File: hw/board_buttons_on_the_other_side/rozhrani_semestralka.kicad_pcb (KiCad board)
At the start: 2 copper layers, 152 x 38.6 mm, 64 parts, among them P1 DISPLAY_CONN, P2 DISPLAY_VCC_CON, P3 USB_B, U1 MCP2210, U2 MIC5504-3.3, U3 Joystick, U4 LM239, U5 CD4532, U6 NPIC6C596, U7 NE555, U8 PB6149L, U9 PB6149L

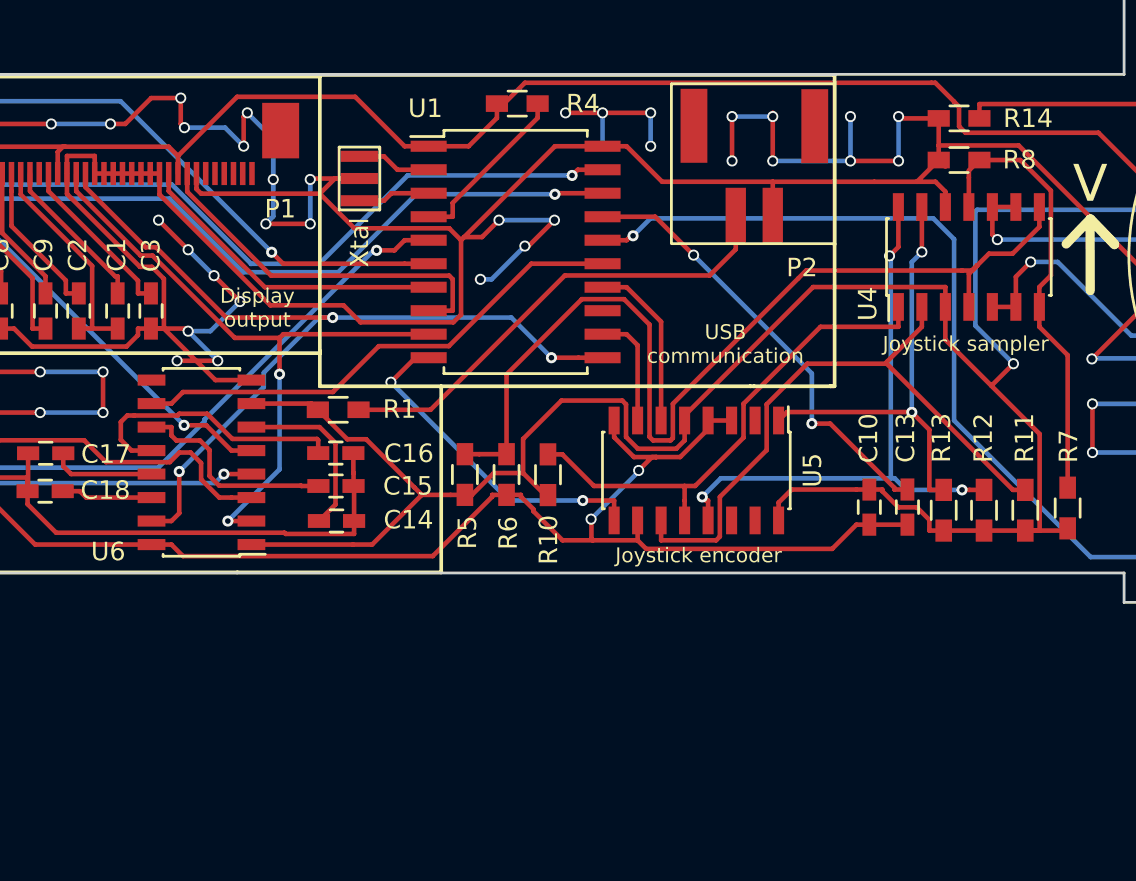
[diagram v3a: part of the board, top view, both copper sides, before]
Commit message: unconnected central button
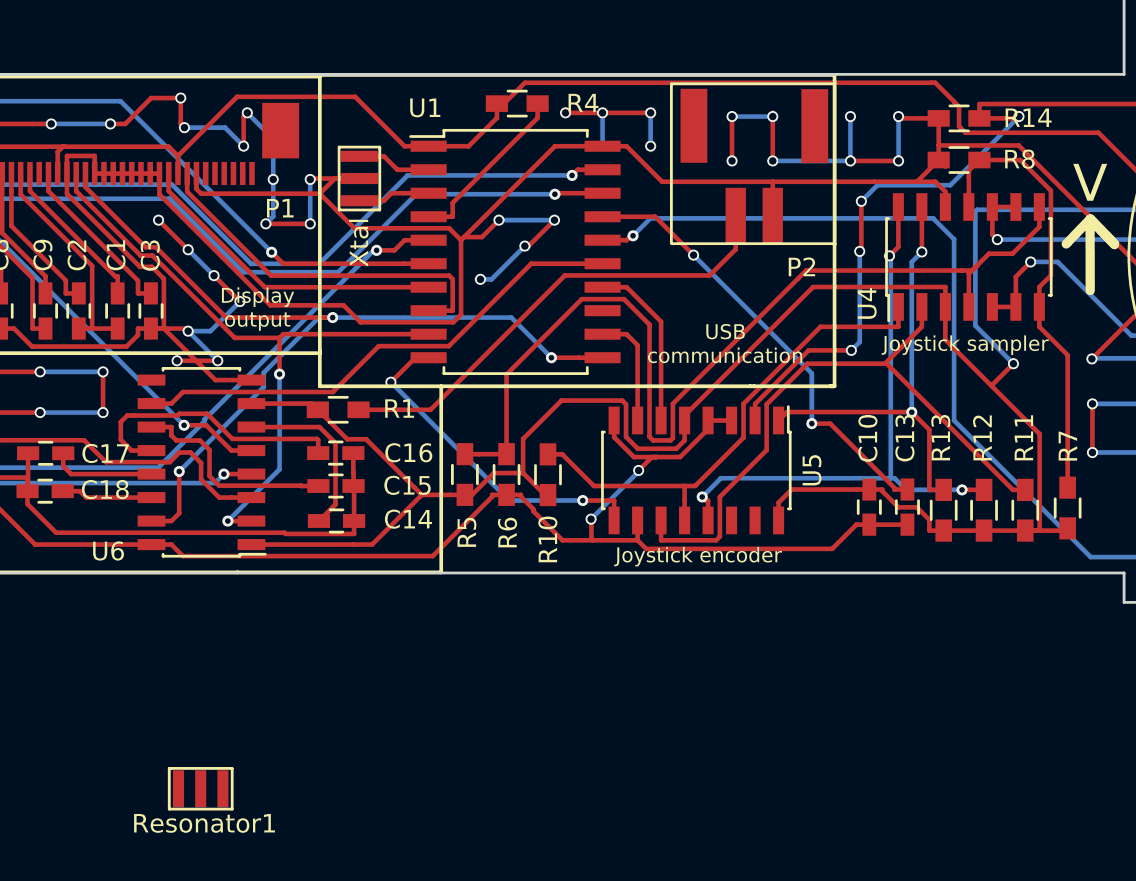
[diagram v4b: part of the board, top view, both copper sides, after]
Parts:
- added Resonator1: 12MHz, pcb:resonator12MHz, F.Cu at (150.7, 131.3)
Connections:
- R14 pad 2: Net-(R14-Pad2) -> /JOY_C
- U3 pad 1: Net-(R14-Pad2) -> /JOY_C
- U3 pad 2: Net-(R14-Pad2) -> /JOY_C
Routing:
- net /JOY_C: track 0.00 -> 54.6 mm, vias 0 -> 4
- net Net-(R14-Pad2): track 26.4 -> 0.00 mm
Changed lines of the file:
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@@
 (kicad_pcb (version 4) (host pcbnew 4.0.2-stable)
   (general
-    (links 0)
-    (no_connects 0)
-    (area 61.976429 80.675 238.433572 122.685)
+    (links 170)
+    (no_connects 3)
+    (area 74.604999 82.624999 226.755001 121.335001)
     (thickness 1.6)
     (drawings 56)
-    (tracks 1166)
+    (tracks 1182)
     (zones 0)
-    (modules 64)
-    (nets 73)
+    (modules 65)
+    (nets 72)
   )
   (page A4)
@@
   )
   (layers
-    (0 F.Cu signal hide)
-    (31 B.Cu signal hide)
+    (0 F.Cu signal)
+    (31 B.Cu signal)
     (32 B.Adhes user)
     (33 F.Adhes user)
@@
   (net 68 GND)
   (net 69 "Net-(C19-Pad1)")
-  (net 70 "Net-(R14-Pad2)")
-  (net 71 "Net-(R21-Pad1)")
-  (net 72 "Net-(R22-Pad2)")
+  (net 70 "Net-(R21-Pad1)")
+  (net 71 "Net-(R22-Pad2)")
   (net_class Default "Toto je výchozí třída sítě."
     (clearance 0.2)
@@
     (add_net "Net-(P1-Pad36)")
     (add_net "Net-(P2-Pad1)")
-    (add_net "Net-(R14-Pad2)")
     (add_net "Net-(R15-Pad1)")
     (add_net "Net-(R17-Pad2)")
@@
       (net 68 GND))
     (pad 2 smd rect (at 1.1 0) (size 1.2 0.9) (layers F.Cu F.Paste F.Mask)
-      (net 70 "Net-(R14-Pad2)"))
+      (net 32 /JOY_C))
     (model Resistors_SMD.3dshapes/R_0603_HandSoldering.wrl
       (at (xyz 0 0 0))
@@
     (fp_circle (center 0 0) (end 12.75 0) (layer F.SilkS) (width 0.15))
     (pad 1 thru_hole circle (at -3 -12.6) (size 1.8 1.8) (drill 1) (layers *.Cu *.SilkS *.Mask)
-      (net 70 "Net-(R14-Pad2)"))
+      (net 32 /JOY_C))
     (pad 2 thru_hole circle (at 3 -12.6) (size 1.8 1.8) (drill 1) (layers *.Cu *.SilkS *.Mask)
-      (net 70 "Net-(R14-Pad2)"))
+      (net 32 /JOY_C))
     (pad 3 thru_hole circle (at -3 -7.6) (size 1.8 1.8) (drill 1) (layers *.Cu *.SilkS *.Mask)
       (net 12 +3V3))
@@
     (fp_line (start -0.5 -0.675) (end 0.5 -0.675) (layer F.SilkS) (width 0.15))
     (pad 1 smd rect (at -1.1 0) (size 1.2 0.9) (layers F.Cu F.Paste F.Mask)
-      (net 71 "Net-(R21-Pad1)"))
+      (net 70 "Net-(R21-Pad1)"))
     (pad 2 smd rect (at 1.1 0) (size 1.2 0.9) (layers F.Cu F.Paste F.Mask)
       (net 38 /REG1))
@@
       (net 39 /REG2))
     (pad 2 smd rect (at 1.1 0 180) (size 1.2 0.9) (layers F.Cu F.Paste F.Mask)
-      (net 72 "Net-(R22-Pad2)"))
+      (net 71 "Net-(R22-Pad2)"))
     (model Resistors_SMD.3dshapes/R_0603_HandSoldering.wrl
       (at (xyz 0 0 0))
@@
       (net 12 +3V3))
     (pad 4 thru_hole circle (at 0 2.7) (size 1.7 1.7) (drill 1) (layers *.Cu *.Mask F.SilkS)
-      (net 71 "Net-(R21-Pad1)"))
+      (net 70 "Net-(R21-Pad1)"))
     (pad 2 thru_hole circle (at 2.54 2.54) (size 1.7 1.7) (drill 1) (layers *.Cu *.Mask F.SilkS)
       (net 51 /BUT1))
@@
       (net 12 +3V3))
     (pad 4 thru_hole circle (at 0 2.7) (size 1.7 1.7) (drill 1) (layers *.Cu *.Mask F.SilkS)
-      (net 72 "Net-(R22-Pad2)"))
+      (net 71 "Net-(R22-Pad2)"))
     (pad 2 thru_hole circle (at 2.54 2.54) (size 1.7 1.7) (drill 1) (layers *.Cu *.Mask F.SilkS)
       (net 52 /BUT2))
@@
       (xy 1.251858 -2.597938)) (layer F.SilkS) (width 0.01))
   )
+  (module pcb:resonator12MHz (layer F.Cu)
+    (at 150.68 131.335001)
+    (fp_text reference Resonator1 (at 0.2 1.9) (layer F.SilkS)
+      (effects (font (size 1 1) (thickness 0.15)))
+    )
+    (fp_text value 12MHz (at 0.7 -2) (layer F.Fab)
+      (effects (font (size 1 1) (thickness 0.15)))
+    )
+    (fp_line (start -1.7 1.1) (end 1.7 1.1) (layer F.SilkS) (width 0.15))
+    (fp_line (start 1.7 1.1) (end 1.7 -1.1) (layer F.SilkS) (width 0.15))
+    (fp_line (start 1.7 -1.1) (end -1.6 -1.1) (layer F.SilkS) (width 0.15))
+    (fp_line (start -1.6 -1.1) (end -1.7 -1.1) (layer F.SilkS) (width 0.15))
+    (fp_line (start -1.7 -1.1) (end -1.7 1.1) (layer F.SilkS) (width 0.15))
+    (pad 3 smd rect (at 0 0) (size 0.6 2) (layers F.Cu F.Paste F.Mask)
+      (net 68 GND))
+    (pad 1 smd rect (at -1.2 0) (size 0.6 2) (layers F.Cu F.Paste F.Mask)
+      (net 28 "Net-(Resonator1-Pad1)"))
+    (pad 2 smd rect (at 1.2 0) (size 0.6 2) (layers F.Cu F.Paste F.Mask)
+      (net 29 "Net-(Resonator1-Pad2)"))
+  )
   (dimension 38.56 (width 0.3) (layer Dwgs.User)
     (gr_text "38,560 mm" (at 61.31 101.98 270) (layer Dwgs.User)
@@
   (segment (start 194.74 103.66) (end 195.54 102.86) (width 0.25) (layer F.Cu) (net 31))
   (segment (start 193.47 105.29) (end 194.74 105.29) (width 0.25) (layer F.Cu) (net 31))
+  (segment (start 180.645 111.43) (end 180.645 110.536298) (width 0.25) (layer F.Cu) (net 32) (status 400000))
+  (segment (start 194.81 95.1) (end 192.77 95.1) (width 0.25) (layer F.Cu) (net 32) (status 800000))
+  (segment (start 194.91 95) (end 194.81 95.1) (width 0.25) (layer F.Cu) (net 32))
+  (via (at 194.91 95) (size 0.6) (drill 0.4) (layers F.Cu B.Cu) (net 32))
+  (segment (start 191.2 98.71) (end 194.91 95) (width 0.25) (layer B.Cu) (net 32))
+  (segment (start 187.26 98.71) (end 191.2 98.71) (width 0.25) (layer B.Cu) (net 32))
+  (segment (start 186.39 99.58) (end 187.26 98.71) (width 0.25) (layer B.Cu) (net 32))
+  (via (at 186.39 99.58) (size 0.6) (drill 0.4) (layers F.Cu B.Cu) (net 32))
+  (segment (start 186.39 102.2) (end 186.39 99.58) (width 0.25) (layer F.Cu) (net 32))
+  (segment (start 186.3 102.29) (end 186.39 102.2) (width 0.25) (layer F.Cu) (net 32))
+  (via (at 186.3 102.29) (size 0.6) (drill 0.4) (layers F.Cu B.Cu) (net 32))
+  (segment (start 186.3 107.19) (end 186.3 102.29) (width 0.25) (layer B.Cu) (net 32))
+  (segment (start 185.85 107.64) (end 186.3 107.19) (width 0.25) (layer B.Cu) (net 32))
+  (via (at 185.85 107.64) (size 0.6) (drill 0.4) (layers F.Cu B.Cu) (net 32))
+  (segment (start 183.541298 107.64) (end 185.85 107.64) (width 0.25) (layer F.Cu) (net 32))
+  (segment (start 180.645 110.536298) (end 183.541298 107.64) (width 0.25) (layer F.Cu) (net 32))
+  (segment (start 192.77 95.1) (end 192.77 94.3247) (width 0.25) (layer F.Cu) (net 32))
+  (segment (start 216.6 89.94) (end 210.6 89.94) (width 0.25) (layer F.Cu) (net 32))
+  (segment (start 206.2153 94.3247) (end 192.77 94.3247) (width 0.25) (layer F.Cu) (net 32))
+  (segment (start 210.6 89.94) (end 206.2153 94.3247) (width 0.25) (layer F.Cu) (net 32))
   (segment (start 176.835 116.83) (end 176.835 115.7547) (width 0.25) (layer F.Cu) (net 33))
   (segment (start 169.45 113.26) (end 170.2253 113.26) (width 0.25) (layer F.Cu) (net 33))
@@
   (segment (start 102.17 115.75) (end 102.17 112.2385) (width 0.25) (layer F.Cu) (net 69))
   (segment (start 102.121 112.1895) (end 102.121 100.1905) (width 0.25) (layer B.Cu) (net 69))
-  (segment (start 192.77 95.1) (end 192.77 94.3247) (width 0.25) (layer F.Cu) (net 70))
-  (segment (start 216.6 89.94) (end 210.6 89.94) (width 0.25) (layer F.Cu) (net 70))
-  (segment (start 206.2153 94.3247) (end 192.77 94.3247) (width 0.25) (layer F.Cu) (net 70))
-  (segment (start 210.6 89.94) (end 206.2153 94.3247) (width 0.25) (layer F.Cu) (net 70))
-  (segment (start 87.47 115.71) (end 92.4 115.71) (width 0.25) (layer F.Cu) (net 71))
-  (segment (start 83.82 119.36) (end 87.47 115.71) (width 0.25) (layer F.Cu) (net 71))
-  (segment (start 88.66 95.97) (end 90.68 95.97) (width 0.25) (layer F.Cu) (net 72))
-  (segment (start 83.82 91.13) (end 88.66 95.97) (width 0.25) (layer F.Cu) (net 72))
+  (segment (start 87.47 115.71) (end 92.4 115.71) (width 0.25) (layer F.Cu) (net 70))
+  (segment (start 83.82 119.36) (end 87.47 115.71) (width 0.25) (layer F.Cu) (net 70))
+  (segment (start 88.66 95.97) (end 90.68 95.97) (width 0.25) (layer F.Cu) (net 71))
+  (segment (start 83.82 91.13) (end 88.66 95.97) (width 0.25) (layer F.Cu) (net 71))
   (zone (net 68) (net_name GND) (layer F.Cu) (hatch edge 0.508)
     (connect_pads (clearance 0.7))

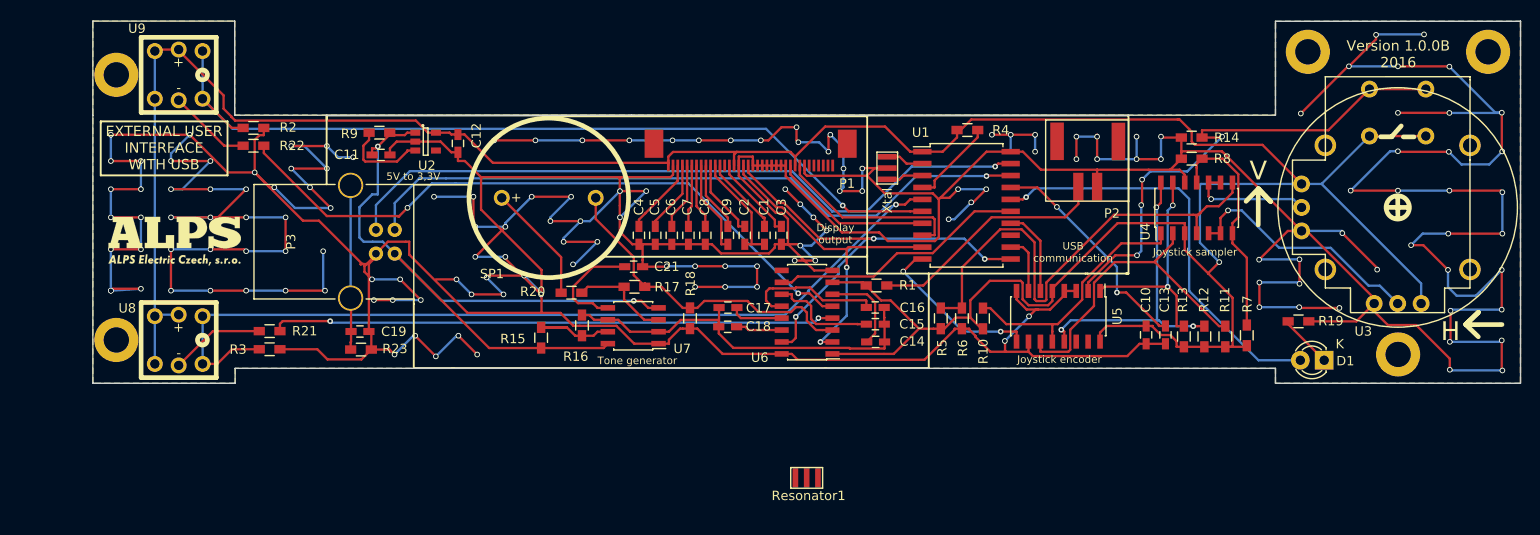
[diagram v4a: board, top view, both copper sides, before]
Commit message: created version 1.1.0 -- usb connector rotated -- there is no compatible with printed casing, please use version 1.0.0B
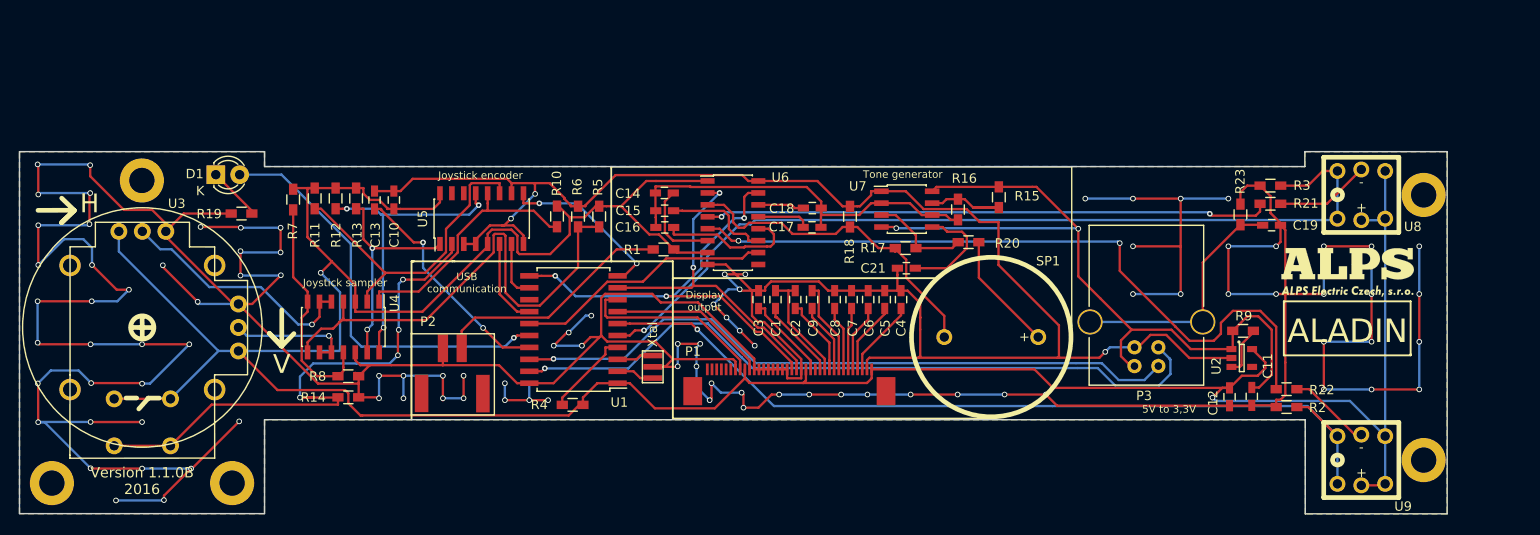
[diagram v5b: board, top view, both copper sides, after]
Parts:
- removed Resonator1: 12MHz, pcb:resonator12MHz
- C14: value 0 -> 1.6nF
- C15: value 0 -> 820pF
- C16: value 0 -> 390pF
- C17: value 0 -> 180pF
- C18: value 0 -> 120pF
- moved REF** 159.7 mm to (70.3, 131.9), turned to 180 degrees
- moved REF** 145.1 mm to (216.4, 129.4), turned to 180 degrees
- moved REF** 140.0 mm to (216.4, 101.2), turned to 180 degrees
- moved REF** 135.0 mm to (79.9, 99.7), turned to 180 degrees
- moved U3 134.3 mm to (80.0, 115.3), turned to 180 degrees
- moved U9 132.4 mm to (209.7, 129.4), turned to 180 degrees
- moved U8 126.9 mm to (209.7, 101.2), turned to 180 degrees
- moved G*** 124.9 mm to (208.3, 109.5)
- moved REF** 123.4 mm to (89.5, 131.9), turned to 180 degrees
- moved D1 119.7 mm to (87.8, 99.0), turned to 0 degrees
- moved R2 113.9 mm to (201.8, 123.8), turned to 0 degrees
- moved R19 113.1 mm to (90.5, 103.2), turned to 0 degrees
- moved R22 113.0 mm to (201.8, 121.9), turned to 0 degrees
- moved R3 108.0 mm to (200.1, 100.2), turned to 180 degrees
- moved R21 107.4 mm to (200.1, 102.2), turned to 180 degrees
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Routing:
- net GND: track 966.4 -> 779.5 mm, vias 153 -> 97
- net +3V3: track 325.5 -> 336.1 mm, vias 1 -> 2
- net Net-(C19-Pad1): track 17.5 -> 26.4 mm
- net /JOY_C: track 54.6 -> 61.3 mm
- net /REG2: track 71.1 -> 76.6 mm
- net VCC: track 79.1 -> 83.4 mm
- net Net-(R9-Pad2): track 9.27 -> 5.34 mm
- net /USB_D+: track 75.6 -> 77.0 mm
- net /BUT1: track 93.6 -> 94.3 mm
- net /SCK: track 48.6 -> 49.2 mm
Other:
- outline, holes or cut-outs redrawn
- board text added: "ALADIN"
- board text added: "Version 1.1.0B 2016"
- board text removed: "EXTERNAL USER INTERFACE WITH USB"
- board text removed: "Version 1.0.0B 2016"

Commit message: Eddited board to version 1.1.1 - now one of button has choise for 2 colour also added values to silk screen
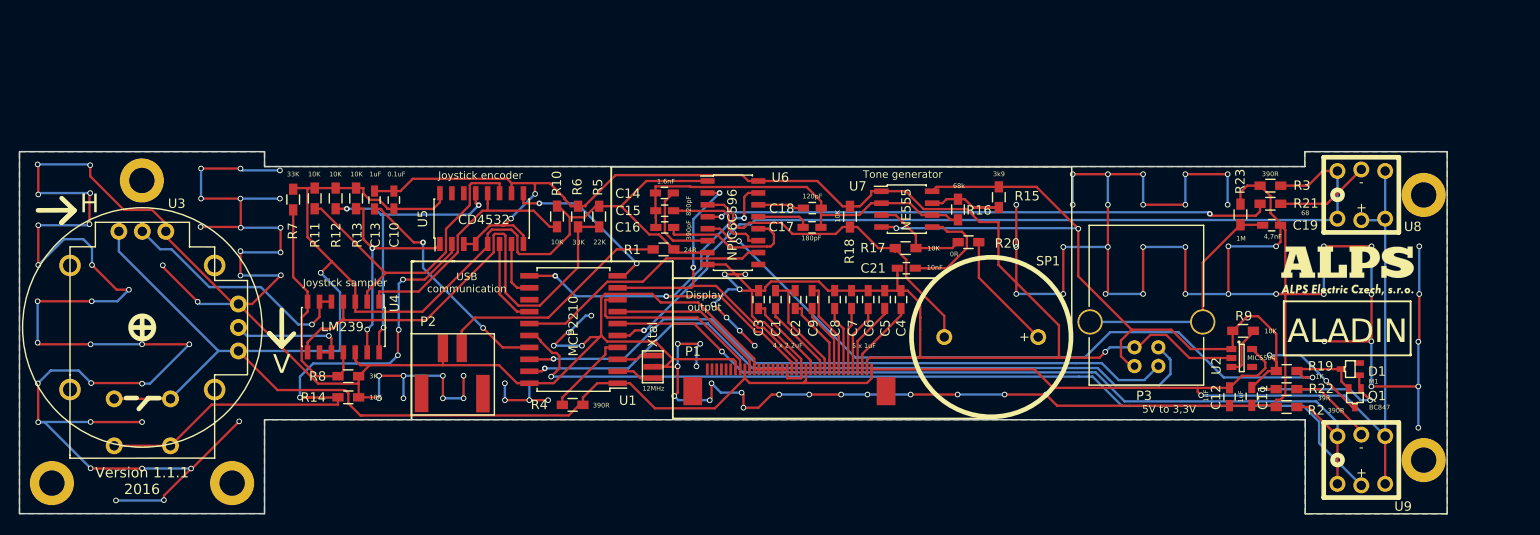
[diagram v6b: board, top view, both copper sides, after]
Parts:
- added Q1: BC847, TO_SOT_Packages_SMD:SOT-323, F.Cu at (209.1, 122.8)
- D1: value L-1334SRT -> M1; footprint LEDs:LED-3MM -> TO_SOT_Packages_SMD:SOT-323
- R1: value 24 -> 24R
- R19: value 390R -> 1K
- R2, R3, R4: value 390 -> 390R
- R22: value 68 -> 39R
- U2: value MIC5504-3.3 -> MIC5504
- U9: value PB6149L -> PB6149Ldual
- moved D1 122.6 mm to (208.6, 119.8), turned to 270 degrees
- moved R19 112.5 mm to (201.8, 120.0), turned to 180 degrees
- moved G*** 0.16 mm to (208.3, 109.3)
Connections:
- D1 pad 1: Net-(D1-Pad1) -> /BUT_LED
- D1 pad 2: /SIGNAL_LED -> (no net)
- P1 pad 13: Net-(P1-Pad13) -> (no net)
- P1 pad 31: Net-(P1-Pad31) -> (no net)
- P1 pad 32: Net-(P1-Pad32) -> (no net)
- P1 pad 33: Net-(P1-Pad33) -> (no net)
- P1 pad 34: Net-(P1-Pad34) -> (no net)
- P1 pad 35: Net-(P1-Pad35) -> (no net)
- P1 pad 36: Net-(P1-Pad36) -> (no net)
- R19 pad 1: GND -> /REG2
- R19 pad 2: Net-(D1-Pad1) -> VCC
- R22 pad 1: /REG2 -> /BUT_LED
- U1 pad 13: /MISO -> (no net)
- U2 pad 4: Net-(U2-Pad4) -> (no net)
- U5 pad 14: Net-(U5-Pad14) -> (no net)
- U5 pad 15: Net-(U5-Pad15) -> (no net)
- U6 pad 9: Net-(U6-Pad9) -> (no net)
- U9 pad 3: +3V3 -> /SIGNAL_LED
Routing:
- net GND: track 779.5 -> 850.8 mm, vias 97 -> 118
- net /SIGNAL_LED: track 44.7 -> 99.2 mm
- net /BUT_LED: track 0.00 -> 16.5 mm, vias 0 -> 2
- net VCC: track 83.4 -> 97.5 mm, vias 2 -> 4
- net Net-(D1-Pad1): track 6.30 -> 0.00 mm
- net /REG2: track 76.6 -> 82.4 mm
- net +3V3: track 336.1 -> 334.0 mm
- net Net-(R22-Pad2): track 8.86 -> 9.78 mm
- net /BUT2: track 92.3 -> 93.1 mm
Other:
- board text added: "4 x 2.2uF"
- board text added: "5 x 1uF"
- board text added: "Version 1.1.1 2016"
- board text removed: "Version 1.1.0B 2016"
